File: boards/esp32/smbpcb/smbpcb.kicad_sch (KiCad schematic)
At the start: 66 parts, among them IC1 MiCS-6814, J1 USB_B_Micro, J2 PMS7003, Q1 SUD08P06-155L, Q2 SS8050_NPN, Q3 SS8050_NPN, SW1 RESET, SW2 RESET, U1 MCP73831-2-OT, U2 SGM6603-5.0YN6G_TR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

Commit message: switch footprints were wrong..."
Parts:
- C10, C17, C9: mfr_part_num (none) -> oops ordered this in 0805
- C3, C4: LCSC C412617 -> C92797
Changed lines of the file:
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@@
       (effects (font (size 1.27 1.27)) hide)
     )
-    (property "Datasheet" "~" (id 3) (at 131.318 58.166 0)
-      (effects (font (size 1.27 1.27)) hide)
-    )
-    (property "LCSC" "C412617" (id 4) (at 131.318 58.166 0)
+    (property "Datasheet" "" (id 3) (at 131.318 58.166 0)
+      (effects (font (size 1.27 1.27)) hide)
+    )
+    (property "LCSC" "C92797 " (id 4) (at 131.318 58.166 0)
       (effects (font (size 1.27 1.27)) hide)
     )
@@
       (effects (font (size 1.27 1.27)) hide)
     )
-    (property "Datasheet" "~" (id 3) (at 205.994 63.5 0)
-      (effects (font (size 1.27 1.27)) hide)
-    )
-    (property "LCSC" "C412617" (id 4) (at 205.994 63.5 0)
+    (property "Datasheet" "" (id 3) (at 205.994 63.5 0)
+      (effects (font (size 1.27 1.27)) hide)
+    )
+    (property "LCSC" "C92797 " (id 4) (at 205.994 63.5 0)
       (effects (font (size 1.27 1.27)) hide)
     )
@@
     )
     (property "Mouser" "0805X106K250NT" (id 5) (at 222.885 124.46 0)
+      (effects (font (size 1.27 1.27)) hide)
+    )
+    (property "mfr_part_num" "oops ordered this in 0805" (id 4) (at 222.885 124.46 0)
       (effects (font (size 1.27 1.27)) hide)
     )
@@
       (effects (font (size 1.27 1.27)) hide)
     )
+    (property "mfr_part_num" "oops ordered this in 0805" (id 4) (at 298.196 72.39 0)
+      (effects (font (size 1.27 1.27)) hide)
+    )
     (pin "1")
     (pin "2")
@@
       (effects (font (size 1.27 1.27)) hide)
     )
+    (property "mfr_part_num" "oops ordered this in 0805" (id 4) (at 303.276 72.39 0)
+      (effects (font (size 1.27 1.27)) hide)
+    )

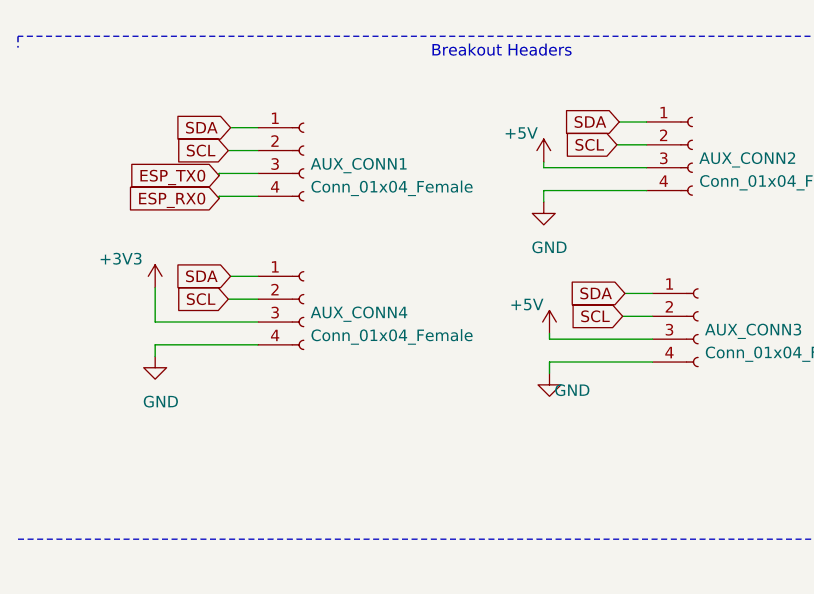
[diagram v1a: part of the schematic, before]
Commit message: swapped header order to be more standard
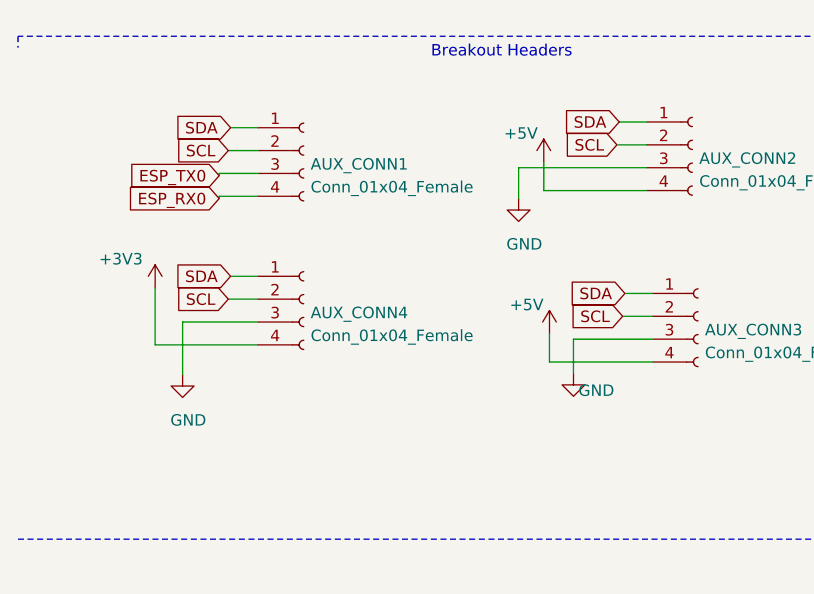
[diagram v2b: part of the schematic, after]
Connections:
- net +3V3: now also AUX_CONN4.4 (Pin_4); no longer AUX_CONN4.3 (Pin_3)
- net +5V: now also AUX_CONN2.4 (Pin_4), AUX_CONN3.4 (Pin_4); no longer AUX_CONN2.3 (Pin_3), AUX_CONN3.3 (Pin_3)
- net GND: now also AUX_CONN2.3 (Pin_3), AUX_CONN3.3 (Pin_3), AUX_CONN4.3 (Pin_3); no longer AUX_CONN2.4 (Pin_4), AUX_CONN3.4 (Pin_4), AUX_CONN4.4 (Pin_4)
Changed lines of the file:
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@@
     (stroke (width 0) (type solid) (color 0 0 0 0))
   )
-  (wire (pts (xy 25.4 124.46) (xy 25.4 128.27))
-    (stroke (width 0) (type solid) (color 0 0 0 0))
-  )
-  (wire (pts (xy 25.4 128.27) (xy 36.83 128.27))
-    (stroke (width 0) (type solid) (color 0 0 0 0))
-  )
-  (wire (pts (xy 25.4 130.81) (xy 25.4 132.08))
-    (stroke (width 0) (type solid) (color 0 0 0 0))
-  )
-  (wire (pts (xy 25.4 130.81) (xy 36.83 130.81))
+  (wire (pts (xy 25.4 130.81) (xy 25.4 124.46))
+    (stroke (width 0) (type solid) (color 0 0 0 0))
+  )
+  (wire (pts (xy 28.448 128.27) (xy 28.448 134.112))
     (stroke (width 0) (type solid) (color 0 0 0 0))
   )
@@
     (stroke (width 0) (type solid) (color 0 0 0 0))
   )
+  (wire (pts (xy 36.83 128.27) (xy 28.448 128.27))
+    (stroke (width 0) (type solid) (color 0 0 0 0))
+  )
+  (wire (pts (xy 36.83 130.81) (xy 25.4 130.81))
+    (stroke (width 0) (type solid) (color 0 0 0 0))
+  )
   (wire (pts (xy 40.005 39.37) (xy 33.02 39.37))
     (stroke (width 0) (type solid) (color 0 0 0 0))
@@
     (stroke (width 0) (type solid) (color 0 0 0 0))
   )
-  (wire (pts (xy 68.58 111.125) (xy 68.58 110.49))
-    (stroke (width 0) (type solid) (color 0 0 0 0))
-  )
-  (wire (pts (xy 68.58 111.125) (xy 80.01 111.125))
-    (stroke (width 0) (type solid) (color 0 0 0 0))
-  )
-  (wire (pts (xy 68.58 113.665) (xy 68.58 114.935))
-    (stroke (width 0) (type solid) (color 0 0 0 0))
-  )
-  (wire (pts (xy 68.58 113.665) (xy 80.01 113.665))
-    (stroke (width 0) (type solid) (color 0 0 0 0))
-  )
-  (wire (pts (xy 69.215 130.175) (xy 69.215 129.54))
-    (stroke (width 0) (type solid) (color 0 0 0 0))
-  )
-  (wire (pts (xy 69.215 130.175) (xy 80.645 130.175))
-    (stroke (width 0) (type solid) (color 0 0 0 0))
-  )
-  (wire (pts (xy 69.215 132.715) (xy 69.215 133.985))
-    (stroke (width 0) (type solid) (color 0 0 0 0))
-  )
-  (wire (pts (xy 69.215 132.715) (xy 80.645 132.715))
+  (wire (pts (xy 65.786 111.125) (xy 65.786 114.554))
+    (stroke (width 0) (type solid) (color 0 0 0 0))
+  )
+  (wire (pts (xy 68.58 113.665) (xy 68.58 110.49))
+    (stroke (width 0) (type solid) (color 0 0 0 0))
+  )
+  (wire (pts (xy 69.215 132.715) (xy 69.215 129.54))
+    (stroke (width 0) (type solid) (color 0 0 0 0))
+  )
+  (wire (pts (xy 71.882 130.175) (xy 71.882 133.985))
     (stroke (width 0) (type solid) (color 0 0 0 0))
   )
@@
   )
   (wire (pts (xy 77.597 125.095) (xy 80.645 125.095))
+    (stroke (width 0) (type solid) (color 0 0 0 0))
+  )
+  (wire (pts (xy 80.01 111.125) (xy 65.786 111.125))
+    (stroke (width 0) (type solid) (color 0 0 0 0))
+  )
+  (wire (pts (xy 80.01 113.665) (xy 68.58 113.665))
+    (stroke (width 0) (type solid) (color 0 0 0 0))
+  )
+  (wire (pts (xy 80.645 130.175) (xy 71.882 130.175))
+    (stroke (width 0) (type solid) (color 0 0 0 0))
+  )
+  (wire (pts (xy 80.645 132.715) (xy 69.215 132.715))
     (stroke (width 0) (type solid) (color 0 0 0 0))
   )
@@
     (pin "1")
   )
-  (symbol (lib_id "power:GND") (at 25.4 132.08 0) (unit 1)
-    (in_bom yes) (on_board yes)
-    (property "Reference" "#PWR0131" (id 0) (at 25.4 138.43 0)
-      (effects (font (size 1.27 1.27)) hide)
-    )
-    (property "Value" "GND" (id 1) (at 26.035 137.16 0))
-    (property "Footprint" "" (id 2) (at 25.4 132.08 0)
-      (effects (font (size 1.27 1.27)) hide)
-    )
-    (property "Datasheet" "" (id 3) (at 25.4 132.08 0)
+  (symbol (lib_id "power:GND") (at 28.448 134.112 0) (unit 1)
+    (in_bom yes) (on_board yes)
+    (property "Reference" "#PWR0131" (id 0) (at 28.448 140.462 0)
+      (effects (font (size 1.27 1.27)) hide)
+    )
+    (property "Value" "GND" (id 1) (at 29.083 139.192 0))
+    (property "Footprint" "" (id 2) (at 28.448 134.112 0)
+      (effects (font (size 1.27 1.27)) hide)
+    )
+    (property "Datasheet" "" (id 3) (at 28.448 134.112 0)
       (effects (font (size 1.27 1.27)) hide)
     )
@@
     (pin "1")
   )
-  (symbol (lib_id "power:GND") (at 68.58 114.935 0) (unit 1)
-    (in_bom yes) (on_board yes)
-    (property "Reference" "#PWR0127" (id 0) (at 68.58 121.285 0)
-      (effects (font (size 1.27 1.27)) hide)
-    )
-    (property "Value" "GND" (id 1) (at 69.215 120.015 0))
-    (property "Footprint" "" (id 2) (at 68.58 114.935 0)
-      (effects (font (size 1.27 1.27)) hide)
-    )
-    (property "Datasheet" "" (id 3) (at 68.58 114.935 0)
-      (effects (font (size 1.27 1.27)) hide)
-    )
-    (pin "1")
-  )
-  (symbol (lib_id "power:GND") (at 69.215 133.985 0) (unit 1)
-    (in_bom yes) (on_board yes)
-    (property "Reference" "#PWR0128" (id 0) (at 69.215 140.335 0)
-      (effects (font (size 1.27 1.27)) hide)
-    )
-    (property "Value" "GND" (id 1) (at 71.755 135.89 0))
-    (property "Footprint" "" (id 2) (at 69.215 133.985 0)
-      (effects (font (size 1.27 1.27)) hide)
-    )
-    (property "Datasheet" "" (id 3) (at 69.215 133.985 0)
-      (effects (font (size 1.27 1.27)) hide)
-    )
+  (symbol (lib_id "power:GND") (at 65.786 114.554 0) (unit 1)
+    (in_bom yes) (on_board yes)
+    (property "Reference" "#PWR0127" (id 0) (at 65.786 120.904 0)
+      (effects (font (size 1.27 1.27)) hide)
+    )
+    (property "Value" "GND" (id 1) (at 66.421 119.634 0))
+    (property "Footprint" "" (id 2) (at 65.786 114.554 0)
+      (effects (font (size 1.27 1.27)) hide)
+    )
+    (property "Datasheet" "" (id 3) (at 65.786 114.554 0)
+      (effects (font (size 1.27 1.27)) hide)
+    )
+    (pin "1")
+  )
+  (symbol (lib_id "power:GND") (at 71.882 133.985 0) (unit 1)
+    (in_bom yes) (on_board yes)
+    (property "Reference" "#PWR0128" (id 0) (at 71.882 140.335 0)
+      (effects (font (size 1.27 1.27)) hide)
+    )
+    (property "Value" "GND" (id 1) (at 74.422 135.89 0))
+    (property "Footprint" "" (id 2) (at 71.882 133.985 0)
+      (effects (font (size 1.27 1.27)) hide)
+    )
+    (property "Datasheet" "" (id 3) (at 71.882 133.985 0)
+      (effects (font (size 1.27 1.27)) hide)
+    )

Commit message: pulled up io0 instaed of en. dhmu
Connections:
- net +3V3: now also R27.2; no longer R27.1
- net EN: now also R27.1
- net IO0: no longer R27.2
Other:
- moved on the sheet: R27
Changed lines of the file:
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@@
   (junction (at 192.405 168.91) (diameter 0.9144) (color 0 0 0 0))
   (junction (at 198.12 53.975) (diameter 0.9144) (color 0 0 0 0))
-  (junction (at 201.93 138.43) (diameter 0.9144) (color 0 0 0 0))
+  (junction (at 201.93 103.632) (diameter 0.9144) (color 0 0 0 0))
   (junction (at 205.994 58.42) (diameter 0.9144) (color 0 0 0 0))
   (junction (at 205.994 84.455) (diameter 0.9144) (color 0 0 0 0))
   (junction (at 212.09 58.42) (diameter 0.9144) (color 0 0 0 0))
-  (junction (at 215.265 120.65) (diameter 0.9144) (color 0 0 0 0))
+  (junction (at 215.138 120.65) (diameter 0.9144) (color 0 0 0 0))
   (junction (at 222.885 120.65) (diameter 0.9144) (color 0 0 0 0))
   (junction (at 251.46 167.005) (diameter 0.9144) (color 0 0 0 0))
@@
     (stroke (width 0) (type solid) (color 0 0 0 0))
   )
-  (wire (pts (xy 201.93 100.33) (xy 201.93 105.41))
-    (stroke (width 0) (type solid) (color 0 0 0 0))
-  )
-  (wire (pts (xy 201.93 135.89) (xy 201.93 138.43))
-    (stroke (width 0) (type solid) (color 0 0 0 0))
-  )
-  (wire (pts (xy 201.93 138.43) (xy 201.93 141.605))
-    (stroke (width 0) (type solid) (color 0 0 0 0))
-  )
-  (wire (pts (xy 201.93 138.43) (xy 215.265 138.43))
+  (wire (pts (xy 201.93 100.33) (xy 201.93 103.632))
+    (stroke (width 0) (type solid) (color 0 0 0 0))
+  )
+  (wire (pts (xy 201.93 103.632) (xy 201.93 105.41))
+    (stroke (width 0) (type solid) (color 0 0 0 0))
+  )
+  (wire (pts (xy 201.93 103.632) (xy 215.138 103.632))
+    (stroke (width 0) (type solid) (color 0 0 0 0))
+  )
+  (wire (pts (xy 201.93 135.89) (xy 201.93 141.605))
     (stroke (width 0) (type solid) (color 0 0 0 0))
   )
@@
     (stroke (width 0) (type solid) (color 0 0 0 0))
   )
+  (wire (pts (xy 207.01 120.65) (xy 215.138 120.65))
+    (stroke (width 0) (type solid) (color 0 0 0 0))
+  )
   (wire (pts (xy 212.09 58.42) (xy 205.994 58.42))
     (stroke (width 0) (type solid) (color 0 0 0 0))
@@
     (stroke (width 0) (type solid) (color 0 0 0 0))
   )
-  (wire (pts (xy 215.265 120.65) (xy 207.01 120.65))
-    (stroke (width 0) (type solid) (color 0 0 0 0))
-  )
-  (wire (pts (xy 215.265 120.65) (xy 215.265 125.095))
-    (stroke (width 0) (type solid) (color 0 0 0 0))
-  )
-  (wire (pts (xy 215.265 120.65) (xy 222.885 120.65))
-    (stroke (width 0) (type solid) (color 0 0 0 0))
-  )
-  (wire (pts (xy 215.265 138.43) (xy 215.265 132.715))
+  (wire (pts (xy 215.138 103.632) (xy 215.138 105.918))
+    (stroke (width 0) (type solid) (color 0 0 0 0))
+  )
+  (wire (pts (xy 215.138 113.538) (xy 215.138 120.65))
+    (stroke (width 0) (type solid) (color 0 0 0 0))
+  )
+  (wire (pts (xy 215.138 120.65) (xy 222.885 120.65))
     (stroke (width 0) (type solid) (color 0 0 0 0))
   )
@@
     (pin "2")
   )
-  (symbol (lib_id "Device:R") (at 215.265 128.905 0) (unit 1)
-    (in_bom yes) (on_board yes)
-    (property "Reference" "R27" (id 0) (at 215.9 125.095 0)
+  (symbol (lib_id "Device:R") (at 215.138 109.728 0) (unit 1)
+    (in_bom yes) (on_board yes)
+    (property "Reference" "R27" (id 0) (at 215.773 105.918 0)
       (effects (font (size 1.27 1.27)) (justify left))
     )
-    (property "Value" "5.1k" (id 1) (at 215.9 132.715 0)
+    (property "Value" "5.1k" (id 1) (at 215.773 113.538 0)
       (effects (font (size 1.27 1.27)) (justify left))
     )
-    (property "Footprint" "Capacitor_SMD:C_0805_2012Metric" (id 2) (at 213.487 128.905 90)
-      (effects (font (size 1.27 1.27)) hide)
-    )
-    (property "Datasheet" "~" (id 3) (at 215.265 128.905 0)
-      (effects (font (size 1.27 1.27)) hide)
-    )
-    (property "LCSC" "C328405" (id 4) (at 215.265 128.905 0)
-      (effects (font (size 1.27 1.27)) hide)
-    )
-    (property "Mouser" " 71-CRCW06035K10FKEAC " (id 5) (at 215.265 128.905 0)
-      (effects (font (size 1.27 1.27)) hide)
-    )
+    (property "Footprint" "Capacitor_SMD:C_0805_2012Metric" (id 2) (at 213.36 109.728 90)
+      (effects (font (size 1.27 1.27)) hide)
+    )
+    (property "Datasheet" "~" (id 3) (at 215.138 109.728 0)
+      (effects (font (size 1.27 1.27)) hide)
+    )
+    (property "LCSC" "C328405" (id 4) (at 215.138 109.728 0)
+      (effects (font (size 1.27 1.27)) hide)
+    )
+    (property "Mouser" " 71-CRCW06035K10FKEAC " (id 5) (at 215.138 109.728 0)
+      (effects (font (size 1.27 1.27)) hide)
+    )

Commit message: turns out mhz19b uses 3v3 logic and also uart doesn't work
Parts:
- removed Q2, Q3: SS8050_NPN, mics:sot-23-3, symbol Transistor_BJT:2N3904
- removed R11, R12, R13, R14, R16: 1k, Capacitor_SMD:C_0805_2012Metric, symbol Device:R
- removed R15: 2k, Capacitor_SMD:C_0805_2012Metric, symbol Device:R
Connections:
- net ESP_RX0: now also AUX_CONN1.3 (Pin_3); no longer AUX_CONN1.4 (Pin_4)
- net ESP_RX1: now also U6.2 (RXD)
- net ESP_TX0: now also AUX_CONN1.4 (Pin_4); no longer AUX_CONN1.3 (Pin_3)
- net ESP_TX1: now also U6.3 (TXD)
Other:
- note removed: "Level switching (this could probably be improved)"

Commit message: mics sucks lol
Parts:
- added R7, R8: 220k, Capacitor_SMD:C_0805_2012Metric, symbol Device:R
- added R9: 68k, Capacitor_SMD:C_0805_2012Metric, symbol Device:R
- R24, R26, R28: Mouser (none) -> RS-05K4700FT
- SW1, SW2: Mouser (none) -> ST-1102W-4.3
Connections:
- net +3V3: now also R22.1; no longer R22.2
- net +5V: now also R7.1, R8.1, R9.1
- net CO: now also R7.2
- net ESP_RX0: now also AUX_CONN1.4 (Pin_4); no longer AUX_CONN1.3 (Pin_3)
- net ESP_RX1: now also AUX_CONN1.2 (Pin_2), U3.36 (IO22); no longer U3.37 (IO23), U6.2 (RXD)
- net ESP_TX0: now also AUX_CONN1.3 (Pin_3); no longer AUX_CONN1.4 (Pin_4)
- net ESP_TX1: now also AUX_CONN1.1 (Pin_1), U3.37 (IO23); no longer U3.36 (IO22), U6.3 (TXD)
- net NH3: now also R8.2
- net NO2: now also R9.2
- net SCL: no longer AUX_CONN1.2 (Pin_2)
- net SDA: no longer AUX_CONN1.1 (Pin_1)
- net at J2.10 (Pin_10): now also R22.2; no longer R22.1
- net pwm_mhz19b: now reaches U6.9 (PWM)
- net pwm_mhz19b: now also U3.33 (IO21)
- no-connect marks 28 -> 26
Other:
- note added: "Auxillary Breakout Headers"
- note removed: "Breakout Headers"
- moved on the sheet: R22, U6
